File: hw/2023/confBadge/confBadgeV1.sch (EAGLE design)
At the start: 94 parts, among them J1 SSW-103-22-F-D-VS-K-TRCON3_SS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, J2 SSW-103-22-F-D-VS-K-TRCON3_SS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, J3 TYPE-C-31-M-12, Q1 8/16/20MHz, U1 ATMEGA328, U10 WS2812-2020, U11 WS2812-2020, U12 WS2812-2020, U13 WS2812-2020, U14 WS2812-2020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

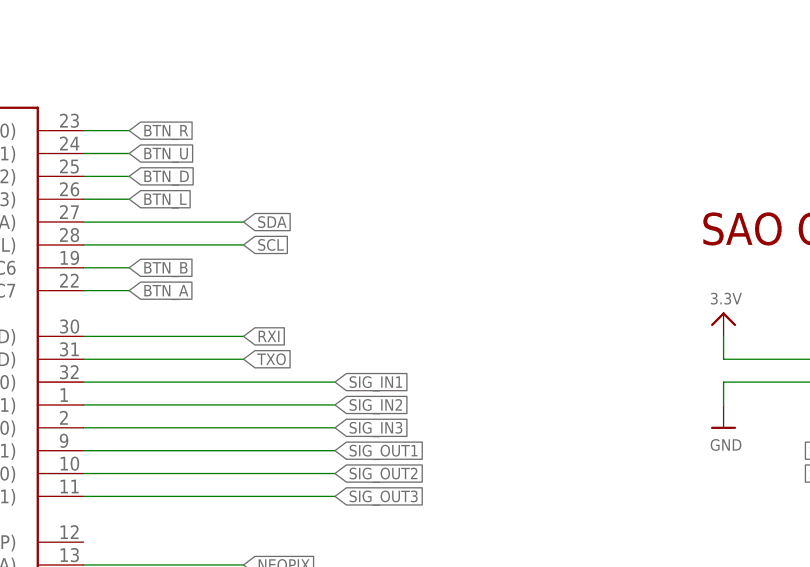
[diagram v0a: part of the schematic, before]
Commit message: generated proposed factory gerber for Rizome (silkscreen still missing)
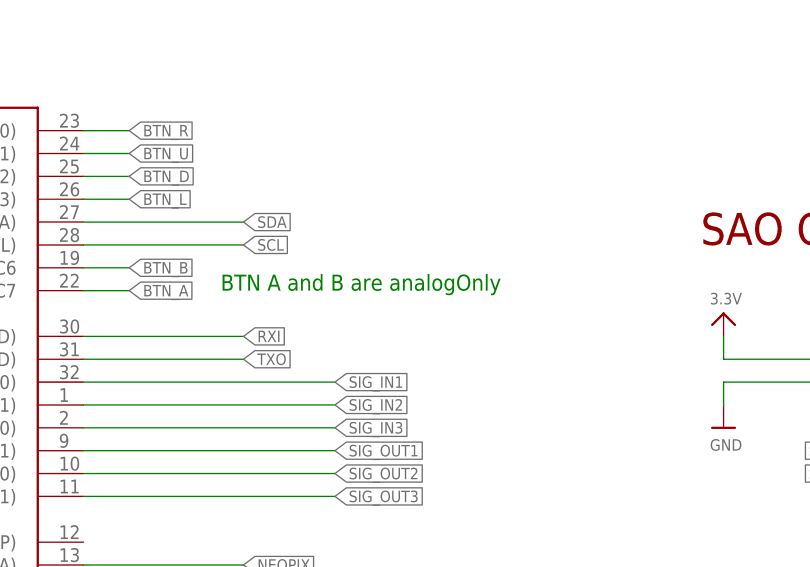
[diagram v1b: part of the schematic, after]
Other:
- note added: "BTN A and B are analogOnly"
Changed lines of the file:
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@@
 <text x="736.6" y="88.9" size="1.778" layer="91">tx
 rx</text>
+<text x="152.4" y="104.14" size="1.778" layer="91">BTN A and B are analogOnly</text>
 </plain>
 <instances>
